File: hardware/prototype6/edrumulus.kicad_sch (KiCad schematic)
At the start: 106 parts, among them J1 Hi-Hat, J10 MIDI-IN, J11 MIDI-OUT, J2 Snare, J3 Crash, J4 Ride, J5 Tom1, J6 Tom2, J7 Tom3, J8 Kick, J9 Hi-Hat-Ctrl, U1 ESP32-DEVKIT-V1, U2 6N138, U3 L78L33_TO92

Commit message: use lower resistors for MIDI out because we have 3.3V
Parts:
- R39: value 220 -> 10
- R41: value 220 -> 33
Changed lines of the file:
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@@
       (effects (font (size 1.27 1.27)) (justify left))
     )
-    (property "Value" "220" (id 1) (at 180.34 52.07 90)
+    (property "Value" "33" (id 1) (at 180.34 52.07 90)
       (effects (font (size 1.27 1.27)) (justify left))
     )
@@
       (effects (font (size 1.27 1.27)) (justify left))
     )
-    (property "Value" "220" (id 1) (at 152.4 57.15 90)
+    (property "Value" "10" (id 1) (at 152.4 57.15 90)
       (effects (font (size 1.27 1.27)) (justify left))
     )
@@
     )
     (path "/f820bba3-f1dc-4a8b-ae09-d5015b75c2a9"
-      (reference "R39") (unit 1) (value "220") (footprint "Resistor_THT:R_Axial_DIN0207_L6.3mm_D2.5mm_P10.16mm_Horizontal")
+      (reference "R39") (unit 1) (value "10") (footprint "Resistor_THT:R_Axial_DIN0207_L6.3mm_D2.5mm_P10.16mm_Horizontal")
     )
     (path "/2ead883a-2ef5-4441-a2ba-3751c5a3785b"
@@
     )
     (path "/53b1f897-371c-47dd-959a-c072a27d4e74"
-      (reference "R41") (unit 1) (value "220") (footprint "Resistor_THT:R_Axial_DIN0207_L6.3mm_D2.5mm_P10.16mm_Horizontal")
+      (reference "R41") (unit 1) (value "33") (footprint "Resistor_THT:R_Axial_DIN0207_L6.3mm_D2.5mm_P10.16mm_Horizontal")
     )
     (path "/40fb713b-3e1b-4ca1-b32b-5a9aea3df735"

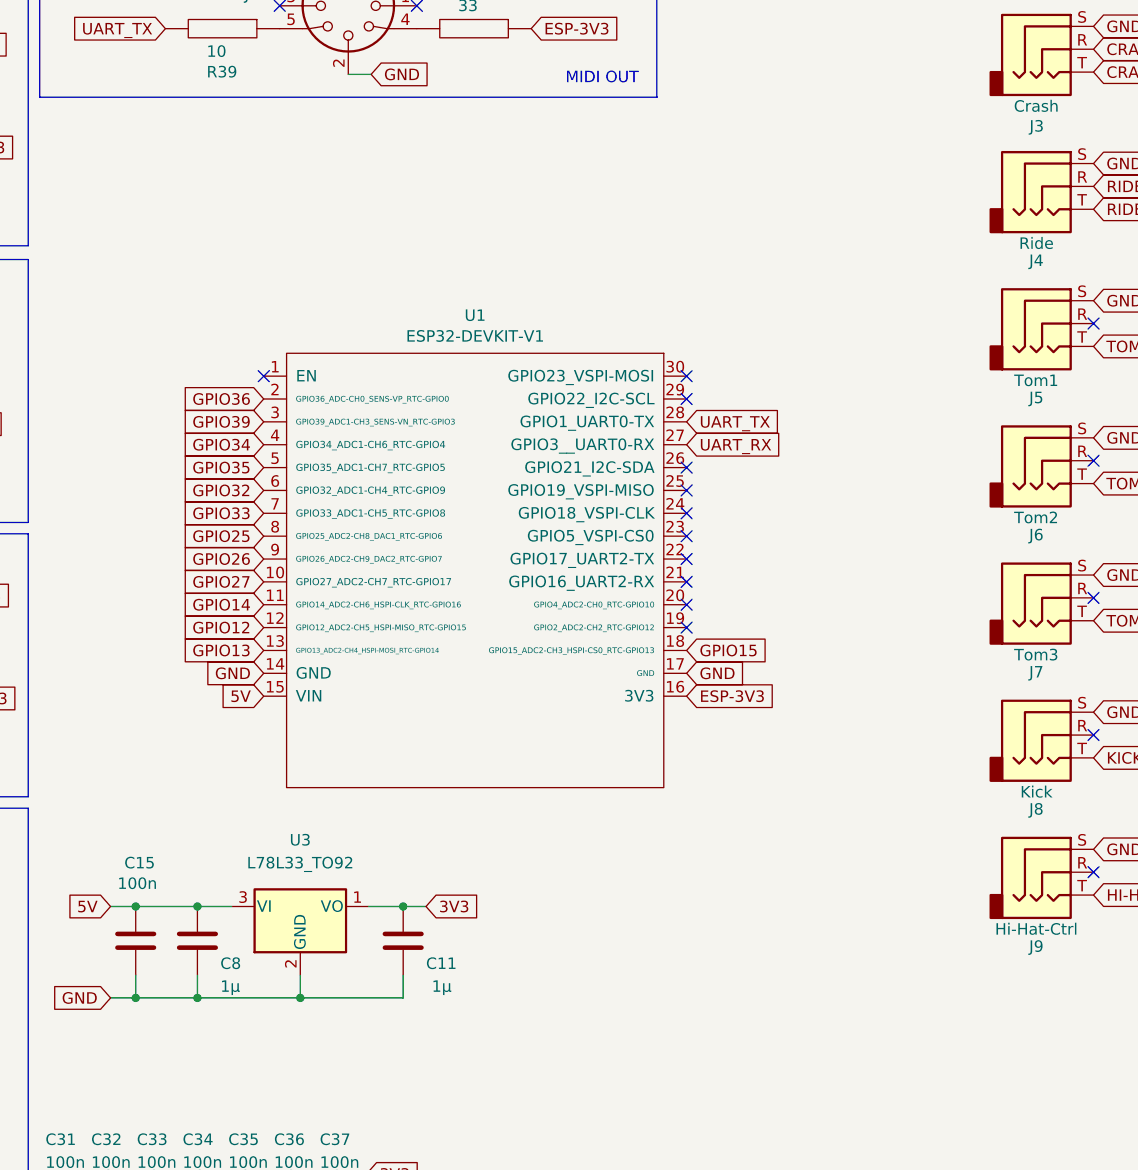
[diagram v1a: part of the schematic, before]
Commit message: change prototype identification for prototype 6
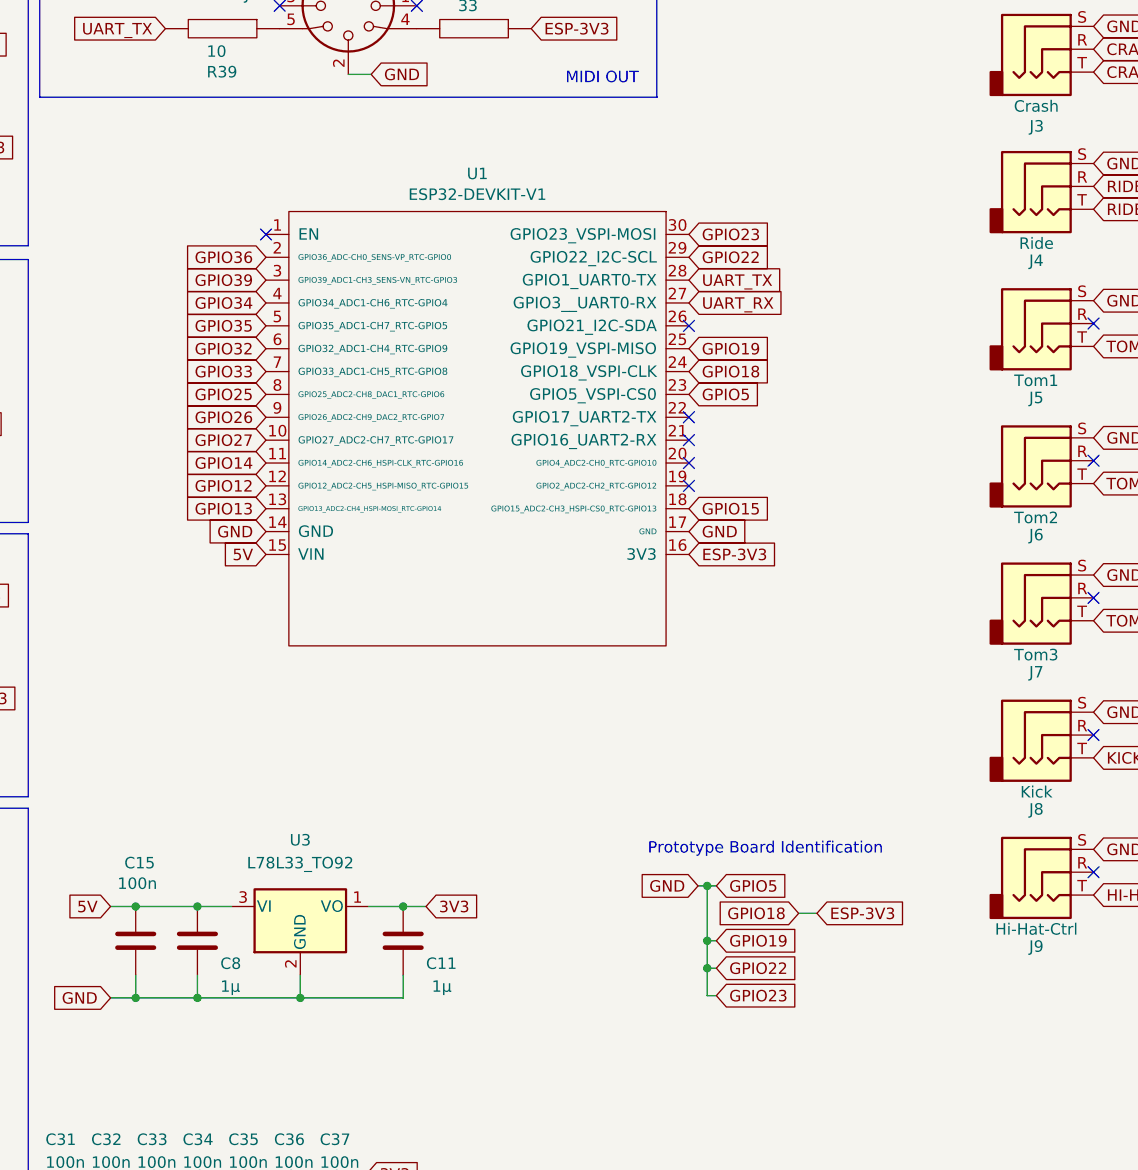
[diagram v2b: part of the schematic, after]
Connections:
- net ESP-3V3: now also U1.24 (GPIO18_VSPI-CLK)
- net GND: now also U1.23 (GPIO5_VSPI-CS0), U1.25 (GPIO19_VSPI-MISO), U1.29 (GPIO22_I2C-SCL), U1.30 (GPIO23_VSPI-MOSI)
- no-connect marks 20 -> 15
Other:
- note added: "Prototype Board Identification"
- moved on the sheet: U1
